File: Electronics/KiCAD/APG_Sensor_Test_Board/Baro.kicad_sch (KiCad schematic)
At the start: 0 parts

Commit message: sensor schematics
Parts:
- added C6: C_Small, symbol Device:C_Small
- added U2: MS5607-02BA, Package_LGA:LGA-8_3x5mm_P1.25mm, symbol Sensor_Pressure:MS5607-02BA
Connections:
- new net +3V3: C6.1, U2.1 (VDD)
- new net CSB: U2.4 (CSB), U2.5 (CSB)
- new net GND: C6.2, U2.2 (PS), U2.3 (GND)
- new net SCLK: U2.8 (SCLK)
- new net SDI: U2.7 (SDI/SDA)
- new net SDO: U2.6 (SDO)

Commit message: Cleaning up schematics
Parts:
- added R3: 0, symbol Device:R
- C6: value C_Small -> 1u
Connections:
- net +3V3: now also R3.1; no longer C6.1, U2.1 (VDD)
- new net: R3.2, U2.1 (VDD)
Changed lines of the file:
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@@
 	(generator_version "8.0")
 	(paper "A4")
-	(junction
-		(at 106.68 54.61)
-		(diameter 0)
-		(color 0 0 0 0)
-	)
-	(junction
-		(at 101.6 63.5)
-		(diameter 0)
-		(color 0 0 0 0)
-	)
-	(wire
-		(pts
-			(xy 106.68 52.07) (xy 106.68 54.61)
-		)
-		(stroke
-			(width 0)
-			(type default)
-		)
-	)
-	(wire
-		(pts
-			(xy 101.6 63.5) (xy 101.6 66.04)
+	(wire
+		(pts
+			(xy 78.74 73.66) (xy 78.74 78.74)
 		)
 		(stroke
@@
 	(wire
 		(pts
-			(xy 96.52 73.66) (xy 93.98 73.66)
-		)
-		(stroke
-			(width 0)
-			(type default)
-		)
-	)
-	(wire
-		(pts
-			(xy 93.98 63.5) (xy 101.6 63.5)
+			(xy 106.68 38.1) (xy 106.68 41.91)
 		)
 		(stroke
@@
 	(wire
 		(pts
+			(xy 78.74 73.66) (xy 96.52 73.66)
+		)
+		(stroke
+			(width 0)
+			(type default)
+		)
+	)
+	(wire
+		(pts
 			(xy 93.98 83.82) (xy 96.52 83.82)
 		)
@@
 	(wire
 		(pts
-			(xy 93.98 73.66) (xy 93.98 63.5)
-		)
-		(stroke
-			(width 0)
-			(type default)
-		)
-	)
-	(wire
-		(pts
-			(xy 106.68 54.61) (xy 106.68 68.58)
+			(xy 106.68 49.53) (xy 106.68 68.58)
 		)
 		(stroke
@@
 			)
 			(justify right)
+		)
+	)
+	(symbol
+		(lib_id "power:GND")
+		(at 78.74 78.74 0)
+		(unit 1)
+		(exclude_from_sim no)
+		(in_bom yes)
+		(on_board yes)
+		(dnp no)
+		(fields_autoplaced yes)
+		(property "Reference" "#PWR017"
+			(at 78.74 85.09 0)
+			(effects
+				(font
+					(size 1.27 1.27)
+				)
+				(hide yes)
+			)
+		)
+		(property "Value" "GND"
+			(at 78.74 83.82 0)
+			(effects
+				(font
+					(size 1.27 1.27)
+				)
+			)
+		)
+		(property "Footprint" ""
+			(at 78.74 78.74 0)
+			(effects
+				(font
+					(size 1.27 1.27)
+				)
+				(hide yes)
+			)
+		)
+		(property "Datasheet" ""
+			(at 78.74 78.74 0)
+			(effects
+				(font
+					(size 1.27 1.27)
+				)
+				(hide yes)
+			)
+		)
+		(property "Description" "Power symbol creates a global label with name \"GND\" , ground"
+			(at 78.74 78.74 0)
+			(effects
+				(font
+					(size 1.27 1.27)
+				)
+				(hide yes)
+			)
+		)
+		(pin "1"
+		)
+		(instances
+			(project ""
+				(path "/3161be0c-372f-463d-be0a-bab00f344057/7b0bc84d-15d8-45fa-9c7e-7492acb184f4"
+					(reference "#PWR017")
+					(unit 1)
+				)
+			)
 		)
 	)
@@
 	)
 	(symbol
+		(lib_id "Device:R")
+		(at 106.68 45.72 0)
+		(unit 1)
+		(exclude_from_sim no)
+		(in_bom yes)
+		(on_board yes)
+		(dnp no)
+		(fields_autoplaced yes)
+		(property "Reference" "R3"
+			(at 109.22 44.4499 0)
+			(effects
+				(font
+					(size 1.27 1.27)
+				)
+				(justify left)
+			)
+		)
+		(property "Value" "0"
+			(at 109.22 46.9899 0)
+			(effects
+				(font
+					(size 1.27 1.27)
+				)
+				(justify left)
+			)
+		)
+		(property "Footprint" ""
+			(at 104.902 45.72 90)
+			(effects
+				(font
+					(size 1.27 1.27)
+				)
+				(hide yes)
+			)
+		)
+		(property "Datasheet" "~"
+			(at 106.68 45.72 0)
+			(effects
+				(font
+					(size 1.27 1.27)
+				)
+				(hide yes)
+			)
+		)
+		(property "Description" "Resistor"
+			(at 106.68 45.72 0)
+			(effects
+				(font
+					(size 1.27 1.27)
+				)
+				(hide yes)
+			)
+		)
+		(pin "1"
+		)
+		(pin "2"
+		)
+		(instances
+			(project ""
+				(path "/3161be0c-372f-463d-be0a-bab00f344057/7b0bc84d-15d8-45fa-9c7e-7492acb184f4"
+					(reference "R3")
+					(unit 1)
+				)
+			)
+		)
+	)
+	(symbol
 		(lib_id "power:GND")
-		(at 101.6 66.04 0)
+		(at 101.6 63.5 0)
 		(unit 1)
 		(exclude_from_sim no)
@@
 		(fields_autoplaced yes)
 		(property "Reference" "#PWR010"
-			(at 101.6 72.39 0)
+			(at 101.6 69.85 0)
 			(effects
 				(font
@@
 		)
 		(property "Value" "GND"
-			(at 101.6 71.12 0)
-			(effects
-				(font
-					(size 1.27 1.27)
-				)
-				(hide yes)
+			(at 101.6 68.58 0)
+			(effects
+				(font
+					(size 1.27 1.27)
+				)
 			)
 		)
 		(property "Footprint" ""
-			(at 101.6 66.04 0)
+			(at 101.6 63.5 0)
 			(effects
 				(font
@@
 		)
 		(property "Datasheet" ""
-			(at 101.6 66.04 0)
+			(at 101.6 63.5 0)
 			(effects
 				(font
@@
 		)
 		(property "Description" "Power symbol creates a global label with name \"GND\" , ground"
-			(at 101.6 66.04 0)
+			(at 101.6 63.5 0)
 			(effects
 				(font
@@
 		)
 		(instances
-			(project "APG_Sensor_Test_Board"
+			(project ""
 				(path "/3161be0c-372f-463d-be0a-bab00f344057/7b0bc84d-15d8-45fa-9c7e-7492acb184f4"
 					(reference "#PWR010")
@@
 	(symbol
 		(lib_id "power:+3V3")
-		(at 106.68 52.07 0)
+		(at 106.68 38.1 0)
 		(unit 1)
 		(exclude_from_sim no)
@@
 		(fields_autoplaced yes)
 		(property "Reference" "#PWR014"
-			(at 106.68 55.88 0)
+			(at 106.68 41.91 0)
 			(effects
 				(font
@@
 		)
 		(property "Value" "+3V3"
-			(at 106.68 46.99 0)
+			(at 106.68 33.02 0)
 			(effects
 				(font
@@
 		)
 		(property "Footprint" ""
-			(at 106.68 52.07 0)
+			(at 106.68 38.1 0)
 			(effects
 				(font
@@
 		)
 		(property "Datasheet" ""
-			(at 106.68 52.07 0)
+			(at 106.68 38.1 0)
 			(effects
 				(font
@@
 		)
 		(property "Description" "Power symbol creates a global label with name \"+3V3\""
-			(at 106.68 52.07 0)
+			(at 106.68 38.1 0)
 			(effects
 				(font
@@
 			)
 		)
-		(property "Value" "C_Small"
+		(property "Value" "1u"
 			(at 99.06 59.6962 0)
 			(effects

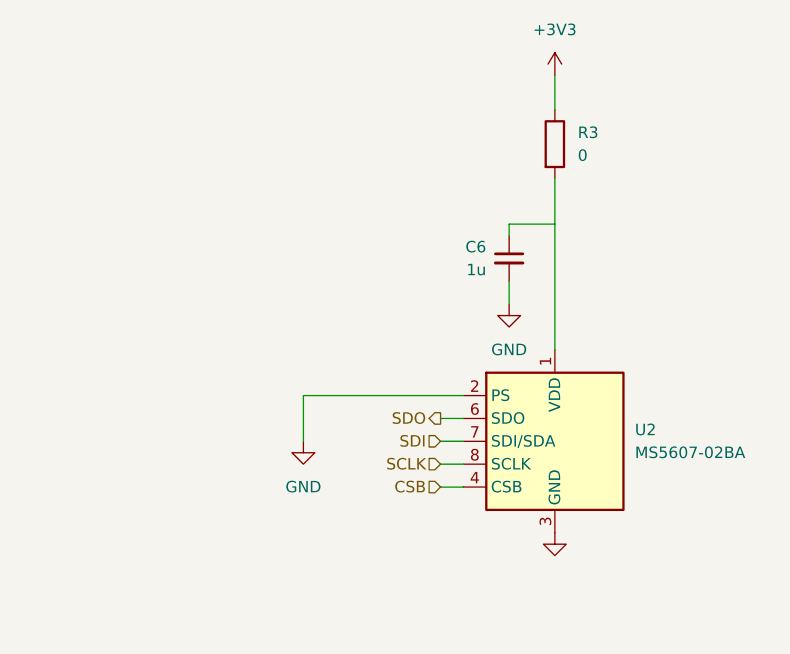
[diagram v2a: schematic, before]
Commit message: Changed IMU and changed sensors to I2C
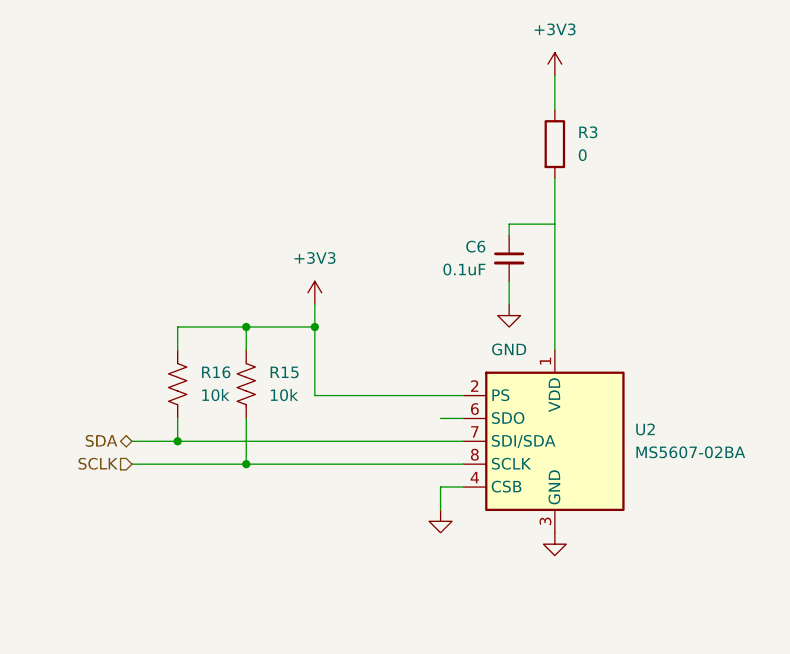
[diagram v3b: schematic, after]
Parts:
- added R15, R16: 10k, symbol Device:R_US
- C6: value 1u -> 0.1uF
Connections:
- net CSB is gone; now on net GND: U2.4 (CSB), U2.5 (CSB)
- net +3V3: now also U2.2 (PS), R15.1, R16.1
- net GND: no longer U2.2 (PS)
- net SCLK: now also R15.2
- net SDI renamed SDA
- net SDA: now also R16.2
- net SDO: no longer names the net of U2.6 (SDO)

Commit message: Main Schematic Complete
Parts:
- removed R15, R16: 10k, symbol Device:R_US
- added R15, R16: 0, symbol Device:R
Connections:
- net +3V3: now also R15.1
- net GND: now also R16.2; no longer U2.4 (CSB), U2.5 (CSB)
- new net: R15.2, R16.1, U2.4 (CSB), U2.5 (CSB)

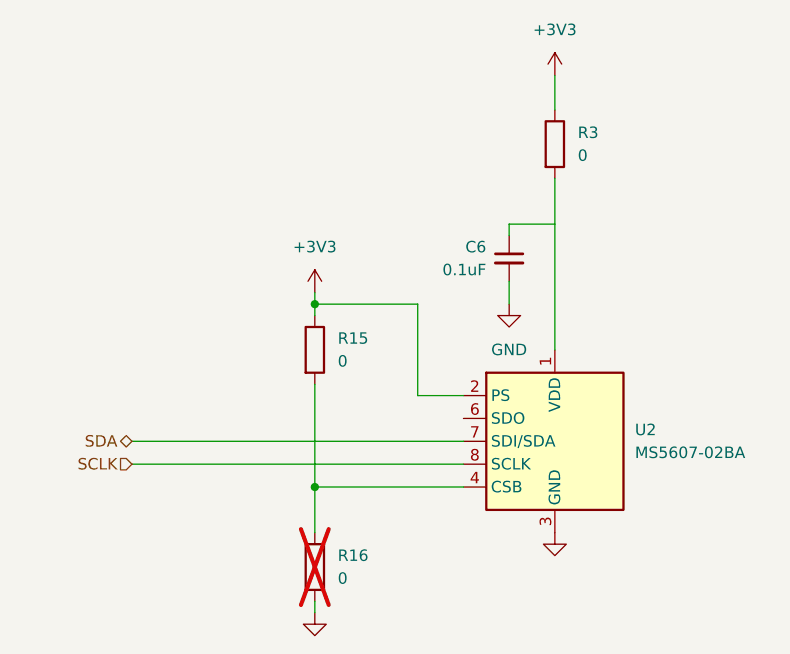
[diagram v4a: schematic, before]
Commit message: reaninotate and begin footprints
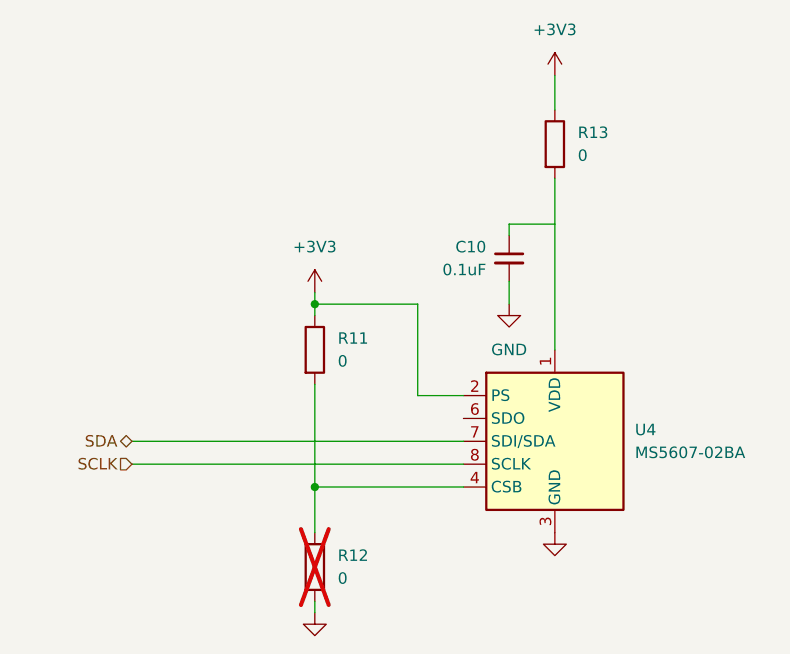
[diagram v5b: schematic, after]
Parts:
- C10: renamed from C6; footprint (none) -> Capacitor_SMD:C_0805_2012Metric
- R11: renamed from R15; footprint (none) -> Resistor_SMD:R_0805_2012Metric
- R12: renamed from R16; footprint (none) -> Resistor_SMD:R_0805_2012Metric
- R13: renamed from R3; footprint (none) -> Resistor_SMD:R_0805_2012Metric
- renumbered U2 to U4
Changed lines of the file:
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@@
 		(dnp no)
 		(fields_autoplaced yes)
-		(property "Reference" "#PWR09"
+		(property "Reference" "#PWR031"
 			(at 106.68 95.25 0)
 			(effects
@@
 			(project ""
 				(path "/3161be0c-372f-463d-be0a-bab00f344057/7b0bc84d-15d8-45fa-9c7e-7492acb184f4"
-					(reference "#PWR09")
+					(reference "#PWR031")
 					(unit 1)
 				)
@@
 		(dnp no)
 		(fields_autoplaced yes)
-		(property "Reference" "#PWR046"
+		(property "Reference" "#PWR028"
 			(at 80.01 104.14 0)
 			(effects
@@
 			(project "APG_Sensor_Test_Board"
 				(path "/3161be0c-372f-463d-be0a-bab00f344057/7b0bc84d-15d8-45fa-9c7e-7492acb184f4"
-					(reference "#PWR046")
+					(reference "#PWR028")
 					(unit 1)
 				)
@@
 		(dnp no)
 		(fields_autoplaced yes)
-		(property "Reference" "R3"
+		(property "Reference" "R13"
 			(at 109.22 44.4499 0)
 			(effects
@@
 			)
 		)
-		(property "Footprint" ""
+		(property "Footprint" "Resistor_SMD:R_0805_2012Metric"
 			(at 104.902 45.72 90)
 			(effects
@@
 			(project ""
 				(path "/3161be0c-372f-463d-be0a-bab00f344057/7b0bc84d-15d8-45fa-9c7e-7492acb184f4"
-					(reference "R3")
+					(reference "R13")
 					(unit 1)
 				)
@@
 		(dnp no)
 		(fields_autoplaced yes)
-		(property "Reference" "#PWR010"
+		(property "Reference" "#PWR029"
 			(at 101.6 69.85 0)
 			(effects
@@
 			(project ""
 				(path "/3161be0c-372f-463d-be0a-bab00f344057/7b0bc84d-15d8-45fa-9c7e-7492acb184f4"
-					(reference "#PWR010")
+					(reference "#PWR029")
 					(unit 1)
 				)
@@
 		(dnp no)
 		(fields_autoplaced yes)
-		(property "Reference" "#PWR017"
+		(property "Reference" "#PWR027"
 			(at 80.01 66.04 0)
 			(effects
@@
 			(project "APG_Sensor_Test_Board"
 				(path "/3161be0c-372f-463d-be0a-bab00f344057/7b0bc84d-15d8-45fa-9c7e-7492acb184f4"
-					(reference "#PWR017")
+					(reference "#PWR027")
 					(unit 1)
 				)
@@
 		(dnp no)
 		(fields_autoplaced yes)
-		(property "Reference" "#PWR014"
+		(property "Reference" "#PWR030"
 			(at 106.68 41.91 0)
 			(effects
@@
 			(project ""
 				(path "/3161be0c-372f-463d-be0a-bab00f344057/7b0bc84d-15d8-45fa-9c7e-7492acb184f4"
-					(reference "#PWR014")
+					(reference "#PWR030")
 					(unit 1)
 				)
@@
 		(dnp yes)
 		(fields_autoplaced yes)
-		(property "Reference" "R16"
+		(property "Reference" "R12"
 			(at 82.55 91.4399 0)
 			(effects
@@
 			)
 		)
-		(property "Footprint" ""
+		(property "Footprint" "Resistor_SMD:R_0805_2012Metric"
 			(at 78.232 92.71 90)
 			(effects
@@
 			(project "APG_Sensor_Test_Board"
 				(path "/3161be0c-372f-463d-be0a-bab00f344057/7b0bc84d-15d8-45fa-9c7e-7492acb184f4"
-					(reference "R16")
+					(reference "R12")
 					(unit 1)
 				)
@@
 		(dnp no)
 		(fields_autoplaced yes)
-		(property "Reference" "U2"
+		(property "Reference" "U4"
 			(at 115.57 77.4699 0)
 			(effects
@@
 			(project ""
 				(path "/3161be0c-372f-463d-be0a-bab00f344057/7b0bc84d-15d8-45fa-9c7e-7492acb184f4"
-					(reference "U2")
+					(reference "U4")
 					(unit 1)
 				)
@@
 		(on_board yes)
 		(dnp no)
-		(property "Reference" "C6"
+		(property "Reference" "C10"
 			(at 99.06 57.1562 0)
 			(effects
@@
 			)
 		)
-		(property "Footprint" ""
+		(property "Footprint" "Capacitor_SMD:C_0805_2012Metric"
 			(at 101.6 58.42 0)
 			(effects
@@
 			(project ""
 				(path "/3161be0c-372f-463d-be0a-bab00f344057/7b0bc84d-15d8-45fa-9c7e-7492acb184f4"
-					(reference "C6")
+					(reference "C10")
 					(unit 1)
 				)
@@
 		(dnp no)
 		(fields_autoplaced yes)
-		(property "Reference" "R15"
+		(property "Reference" "R11"
 			(at 82.55 67.3099 0)
 			(effects
@@
 			)
 		)
-		(property "Footprint" ""
+		(property "Footprint" "Resistor_SMD:R_0805_2012Metric"
 			(at 78.232 68.58 90)
 			(effects
@@
 			(project "APG_Sensor_Test_Board"
 				(path "/3161be0c-372f-463d-be0a-bab00f344057/7b0bc84d-15d8-45fa-9c7e-7492acb184f4"
-					(reference "R15")
-					(unit 1)
-				)
+					(reference "R11")
+					(unit 1)
+				)

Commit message: JLC part numbers
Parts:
- U4: JLCPCB (none) -> C97627
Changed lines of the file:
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@@
+			)
+		)
+		(property "JLCPCB" "C97627"
+			(at 106.68 78.74 0)
+			(effects
+				(font
+					(size 1.27 1.27)
+				)
+				(hide yes)
 			)
 		)

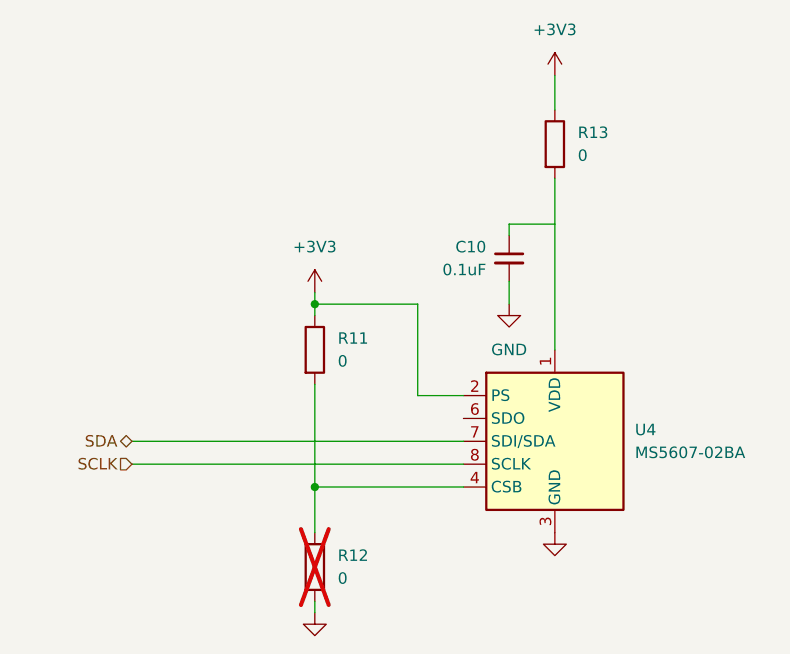
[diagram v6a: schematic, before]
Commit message: MOved IMU and HIGH G to SPI other misc changes
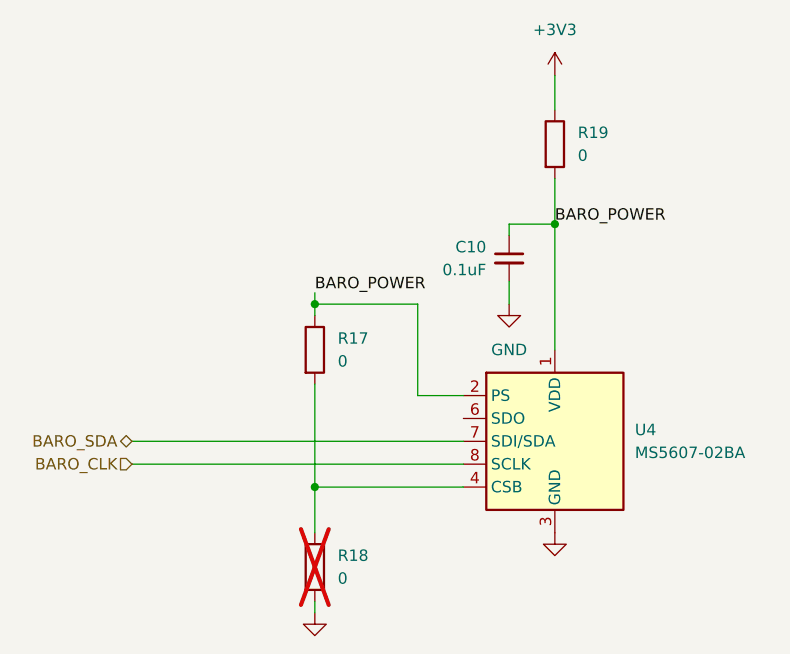
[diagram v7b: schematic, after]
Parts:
- renumbered R11 to R17, R12 to R18, R13 to R19
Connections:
- net +3V3: no longer R17.1, U4.2 (PS)
- net BARO_POWER: now reaches R19.2, U4.1 (VDD)
- net BARO_POWER: now also C10.1, R17.1, U4.2 (PS)
- net SCLK renamed BARO_CLK
- net SDA renamed BARO_SDA
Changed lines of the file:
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@@
 		(color 0 0 0 0)
 	)
+	(junction
+		(at 106.68 54.61)
+		(diameter 0)
+		(color 0 0 0 0)
+	)
 	(wire
 		(pts
@@
 	(wire
 		(pts
-			(xy 106.68 49.53) (xy 106.68 68.58)
+			(xy 106.68 49.53) (xy 106.68 54.61)
 		)
 		(stroke
@@
 	(wire
 		(pts
+			(xy 106.68 54.61) (xy 106.68 68.58)
+		)
+		(stroke
+			(width 0)
+			(type default)
+		)
+	)
+	(wire
+		(pts
 			(xy 59.69 78.74) (xy 96.52 78.74)
 		)
@@
 		)
 	)
-	(hierarchical_label "SCLK"
-		(shape input)
-		(at 59.69 81.28 180)
+	(label "BARO_POWER"
+		(at 106.68 54.61 0)
 		(fields_autoplaced yes)
 		(effects
@@
 				(size 1.27 1.27)
 			)
+			(justify left bottom)
+		)
+	)
+	(label "BARO_POWER"
+		(at 80.01 62.23 0)
+		(fields_autoplaced yes)
+		(effects
+			(font
+				(size 1.27 1.27)
+			)
+			(justify left bottom)
+		)
+	)
+	(hierarchical_label "BARO_CLK"
+		(shape input)
+		(at 59.69 81.28 180)
+		(fields_autoplaced yes)
+		(effects
+			(font
+				(size 1.27 1.27)
+			)
 			(justify right)
 		)
 	)
-	(hierarchical_label "SDA"
+	(hierarchical_label "BARO_SDA"
 		(shape bidirectional)
 		(at 59.69 78.74 180)
@@
 		(dnp no)
 		(fields_autoplaced yes)
-		(property "Reference" "#PWR031"
+		(property "Reference" "#PWR028"
 			(at 106.68 95.25 0)
 			(effects
@@
 			(project ""
 				(path "/3161be0c-372f-463d-be0a-bab00f344057/7b0bc84d-15d8-45fa-9c7e-7492acb184f4"
-					(reference "#PWR031")
+					(reference "#PWR028")
 					(unit 1)
 				)
@@
 		(dnp no)
 		(fields_autoplaced yes)
-		(property "Reference" "#PWR028"
+		(property "Reference" "#PWR025"
 			(at 80.01 104.14 0)
 			(effects
@@
 			(project "APG_Sensor_Test_Board"
 				(path "/3161be0c-372f-463d-be0a-bab00f344057/7b0bc84d-15d8-45fa-9c7e-7492acb184f4"
-					(reference "#PWR028")
+					(reference "#PWR025")
 					(unit 1)
 				)
@@
 		(dnp no)
 		(fields_autoplaced yes)
-		(property "Reference" "R13"
+		(property "Reference" "R19"
 			(at 109.22 44.4499 0)
 			(effects
@@
 			(project ""
 				(path "/3161be0c-372f-463d-be0a-bab00f344057/7b0bc84d-15d8-45fa-9c7e-7492acb184f4"
-					(reference "R13")
+					(reference "R19")
 					(unit 1)
 				)
@@
 		(dnp no)
 		(fields_autoplaced yes)
-		(property "Reference" "#PWR029"
+		(property "Reference" "#PWR026"
 			(at 101.6 69.85 0)
 			(effects
@@
 			(project ""
 				(path "/3161be0c-372f-463d-be0a-bab00f344057/7b0bc84d-15d8-45fa-9c7e-7492acb184f4"
-					(reference "#PWR029")
-					(unit 1)
-				)
-			)
-		)
-	)
-	(symbol
-		(lib_id "power:+3V3")
-		(at 80.01 62.23 0)
-		(unit 1)
-		(exclude_from_sim no)
-		(in_bom yes)
-		(on_board yes)
-		(dnp no)
-		(fields_autoplaced yes)
-		(property "Reference" "#PWR027"
-			(at 80.01 66.04 0)
-			(effects
-				(font
-					(size 1.27 1.27)
-				)
-				(hide yes)
-			)
-		)
-		(property "Value" "+3V3"
-			(at 80.01 57.15 0)
-			(effects
-				(font
-					(size 1.27 1.27)
-				)
-			)
-		)
-		(property "Footprint" ""
-			(at 80.01 62.23 0)
-			(effects
-				(font
-					(size 1.27 1.27)
-				)
-				(hide yes)
-			)
-		)
-		(property "Datasheet" ""
-			(at 80.01 62.23 0)
-			(effects
-				(font
-					(size 1.27 1.27)
-				)
-				(hide yes)
-			)
-		)
-		(property "Description" "Power symbol creates a global label with name \"+3V3\""
-			(at 80.01 62.23 0)
-			(effects
-				(font
-					(size 1.27 1.27)
-				)
-				(hide yes)
-			)
-		)
-		(pin "1"
-		)
-		(instances
-			(project "APG_Sensor_Test_Board"
-				(path "/3161be0c-372f-463d-be0a-bab00f344057/7b0bc84d-15d8-45fa-9c7e-7492acb184f4"
-					(reference "#PWR027")
+					(reference "#PWR026")
 					(unit 1)
 				)
@@
 		(dnp no)
 		(fields_autoplaced yes)
-		(property "Reference" "#PWR030"
+		(property "Reference" "#PWR027"
 			(at 106.68 41.91 0)
 			(effects
@@
 			(project ""
 				(path "/3161be0c-372f-463d-be0a-bab00f344057/7b0bc84d-15d8-45fa-9c7e-7492acb184f4"
-					(reference "#PWR030")
+					(reference "#PWR027")
 					(unit 1)
 				)
@@
 		(dnp yes)
 		(fields_autoplaced yes)
-		(property "Reference" "R12"
+		(property "Reference" "R18"
 			(at 82.55 91.4399 0)
 			(effects
@@
 			(project "APG_Sensor_Test_Board"
 				(path "/3161be0c-372f-463d-be0a-bab00f344057/7b0bc84d-15d8-45fa-9c7e-7492acb184f4"
-					(reference "R12")
+					(reference "R18")
 					(unit 1)
 				)
@@
 		(dnp no)
 		(fields_autoplaced yes)
-		(property "Reference" "R11"
+		(property "Reference" "R17"
 			(at 82.55 67.3099 0)
 			(effects
@@
 			(project "APG_Sensor_Test_Board"
 				(path "/3161be0c-372f-463d-be0a-bab00f344057/7b0bc84d-15d8-45fa-9c7e-7492acb184f4"
-					(reference "R11")
+					(reference "R17")
 					(unit 1)
 				)
